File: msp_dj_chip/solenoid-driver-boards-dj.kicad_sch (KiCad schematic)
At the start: 0 parts

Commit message: updated changes
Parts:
- added C19: C_Small, symbol Device:C_Small
- added Q1: NMOS, symbol Simulation_SPICE:NMOS
- added R48: 30K, symbol Device:R_Small
- added R49: 500, symbol Device:R_Small
- added R50: 1K2, symbol Device:R_Small
- added R51, R52: 1, symbol Device:R_Small
- added R53: 0, symbol Device:R_Small
- added TP2, TP3, TP4, TP5, TP6: TestPoint, symbol Connector:TestPoint
- added U16: ${SIM.PARAMS}, symbol Simulation_SPICE:OPAMP
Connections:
- new net: R48.2, R49.1, TP2.1, U16.1 (+)
- new net: C19.2, Q1.2 (G), R51.2, R53.1, TP5.1
- new net: Q1.1 (D), TP6.1
- new net: C19.1, R53.2, U16.5
- new net: Q1.3 (S), R50.1, R50.2, R52.2, TP3.1, TP4.1, U16.2 (-)
- new net +24V: U16.3 (V+)
- new net GND: R49.2, R51.1, R52.1, U16.4 (V-)

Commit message: SOL-DRIVER-SHEET-ADDED
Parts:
- removed Q1: NMOS, symbol Simulation_SPICE:NMOS
- removed U16: ${SIM.PARAMS}, symbol Simulation_SPICE:OPAMP
- added C20, C21, C22, C23, C24, C25, C26, C27, C28, C29, C30, C31, C32, C33, C34: C_Small, symbol Device:C_Small
- added Q1, Q2, Q3, Q4, Q5, Q6, Q7, Q8: PMGD780SN, project_footprints:PMGD780SN, symbol Project_Symbols:2N-Channel_MOSFET
- added R100, R102, R120, R122, R124, R126, R54, R60, R62, R72, R74, R84, R86, R96, R98: 30K, symbol Device:R_Small
- added R101, R103, R121, R123, R125, R127, R55, R61, R63, R73, R75, R85, R87, R97, R99: 500, symbol Device:R_Small
- added R104, R105, R106, R107, R128, R129, R132, R133, R56, R64, R65, R76, R77, R88, R89: 1K2, symbol Device:R_Small
- added R108, R109, R110, R111, R130, R131, R134, R135, R57, R66, R67, R78, R79, R90, R91: 0, symbol Device:R_Small
- added R112, R113, R114, R115, R116, R117, R118, R119, R136, R137, R138, R139, R140, R141, R142, R143, R58, R59, R68, R69, R70, R71, R80, R81, R82, R83, R92, R93, R94, R95: 1, symbol Device:R_Small
- added TP10, TP11, TP12, TP13, TP14, TP15, TP16, TP17, TP18, TP19, TP20, TP21, TP22, TP23, TP24, TP25, TP26, TP27, TP28, TP29, TP30, TP31, TP32, TP33, TP34, TP35, TP36, TP37, TP38, TP39, TP40, TP41, TP42, TP43, TP44, TP45, TP46, TP47, TP48, TP49, TP50, TP51, TP52, TP53, TP54, TP55, TP56, TP57, TP58, TP59, TP60, TP61, TP62, TP63, TP64, TP65, TP66, TP67, TP68, TP69, TP7, TP70, TP71, TP72, TP73, TP74, TP75, TP76, TP77, TP78, TP79, TP8, TP80, TP81, TP9: TestPoint, symbol Connector:TestPoint
- added U16, U17, U18, U19, U20, U21, U22, U23: NCV272DMR2G, Package_SO:MSOP-8_3x3mm_P0.65mm, symbol Project_Symbols:OpAmp_NCV272
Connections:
- net +24V: now also U16.8 (VDD), U17.8 (VDD), U18.8 (VDD), U19.8 (VDD), U20.8 (VDD), U21.8 (VDD), U22.8 (VDD), U23.8 (VDD)
- net GND: now also R101.2, R103.2, R112.1, R113.1, R114.1, R115.1, R116.1, R117.1, R118.1, R119.1, R121.2, R123.2, R125.2, R127.2, R136.1, R137.1, R138.1, R139.1, R140.1, R141.1, R142.1, R143.1, R55.2, R58.1, R59.1, R61.2, R63.2, R68.1, R69.1, R70.1, R71.1, R73.2, R75.2, R80.1, R81.1, R82.1, R83.1, R85.2, R87.2, R92.1, R93.1, R94.1, R95.1, R97.2, R99.2, U16.4 (VSS), U17.4 (VSS), U18.4 (VSS), U19.4 (VSS), U20.4 (VSS), U21.4 (VSS), U22.4 (VSS), U23.4 (VSS)
- net at R48.2, R49.1, TP2.1: now also U16.2 (IN-1)
- net at C19.2, R51.2, R53.1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: now also Q2.2 (G1)
- net at TP6.1: now also Q2.6 (D1)
- net at C19.1, R53.2: now also U16.1 (OUT_1)
- net at R50.2, R52.2, TP4.1: now also Q2.1 (S1); no longer R50.1, TP3.1
- new net: C23.2, Q3.2 (G1), R78.1, R80.2, TP26.1
- new net: R72.2, R73.1, TP22.1, U18.2 (IN-1)
- new net: R60.2, R61.1, TP12.1, U17.2 (IN-1)
- new net: C21.2, Q1.2 (G1), R66.1, R68.2, TP16.1
- new net: C21.1, R66.2, U17.1 (OUT_1)
- new net: Q4.4 (S2), R89.2, R95.2, TP41.1
- new net: R96.2, R97.1, TP42.1, U20.2 (IN-1)
- new net: C26.2, Q4.5 (G2), R91.1, R93.2, TP37.1
- new net: R128.1, TP66.1, U22.3 (IN+1)
- new net: C25.2, Q4.2 (G1), R90.1, R92.2, TP36.1
- new net: Q3.6 (D1), TP28.1
- new net: R74.2, R75.1, TP23.1, U18.6 (IN-2)
- new net: Q1.6 (D1), TP18.1
- new net: C27.2, Q5.2 (G1), R108.1, R112.2, TP50.1
- new net: C27.1, R108.2, U20.1 (OUT_1)
- new net: R129.1, TP67.1, U22.5 (IN+2)
- new net: Q7.4 (S2), R129.2, R141.2, TP77.1
- new net: R105.1, TP47.1, U20.5 (IN+2)
- new net: Q8.1 (S1), R132.2, R142.2, TP79.1
- new net: C33.2, Q8.2 (G1), R134.1, R138.2, TP72.1
- new net: Q8.6 (D1), TP78.1
- new net: R126.2, R127.1, TP65.1, U23.6 (IN-2)
- new net: C25.1, R90.2, U19.1 (OUT_1)
- new net: R133.1, TP69.1, U23.5 (IN+2)
- new net: C34.1, R135.2, U23.7 (OUT_2)
- new net: R84.2, R85.1, TP32.1, U19.2 (IN-1)
- new net: R88.1, TP34.1, U19.3 (IN+1)
- new net: R89.1, TP35.1, U19.5 (IN+2)
- new net: R86.2, R87.1, TP33.1, U19.6 (IN-2)
- new net: C26.1, R91.2, U19.7 (OUT_2)
- new net: C24.1, R79.2, U18.7 (OUT_2)
- new net: C24.2, Q3.5 (G2), R79.1, R81.2, TP27.1
- new net: R107.1, TP49.1, U21.5 (IN+2)
- new net: R102.2, R103.1, TP45.1, U21.6 (IN-2)
- new net: C30.1, R111.2, U21.7 (OUT_2)
- new net: R76.1, TP24.1, U18.3 (IN+1)
- new net: C22.1, R67.2, U17.7 (OUT_2)
- new net: C22.2, Q1.5 (G2), R67.1, R69.2, TP17.1
- new net: C20.2, Q2.5 (G2), R57.1, R58.2, TP9.1
- new net: C20.1, R57.2, U16.7 (OUT_2)
- new net: Q3.1 (S1), R76.2, R82.2, TP29.1
- new net: Q8.3 (D2), TP80.1
- new net: Q8.4 (S2), R133.2, R143.2, TP81.1
- new net: C34.2, Q8.5 (G2), R135.1, R139.2, TP73.1
- new net: Q6.3 (D2), TP60.1
- new net: R104.1, TP46.1, U20.3 (IN+1)
- new net: C23.1, R78.2, U18.1 (OUT_1)
- new net: Q4.1 (S1), R88.2, R94.2, TP39.1
- new net: Q4.6 (D1), TP38.1
- new net: Q5.6 (D1), TP54.1
- new net: Q6.6 (D1), TP58.1
- new net: Q3.3 (D2), TP30.1
- new net: Q3.4 (S2), R77.2, R83.2, TP31.1
- new net: R98.2, R99.1, TP43.1, U20.6 (IN-2)
- new net: R65.1, TP15.1, U17.5 (IN+2)
- new net: R62.2, R63.1, TP13.1, U17.6 (IN-2)
- new net: Q2.3 (D2), TP10.1
- new net: Q1.4 (S2), R65.2, R71.2, TP21.1
- new net: Q7.1 (S1), R128.2, R140.2, TP75.1
- new net: C31.2, Q7.2 (G1), R130.1, R136.2, TP70.1
- new net: Q7.6 (D1), TP74.1
- new net: R100.2, R101.1, TP44.1, U21.2 (IN-1)
- new net: Q1.1 (S1), R64.2, R70.2, TP19.1
- new net: Q5.1 (S1), R104.2, R116.2, TP55.1
- new net: C33.1, R134.2, U23.1 (OUT_1)
- new net: R124.2, R125.1, TP64.1, U23.2 (IN-1)
- new net: R132.1, TP68.1, U23.3 (IN+1)
- new net: R77.1, TP25.1, U18.5 (IN+2)
- new net: R106.1, TP48.1, U21.3 (IN+1)
- new net: C30.2, Q6.5 (G2), R111.1, R115.2, TP53.1
- new net: R56.1, TP8.1, U16.5 (IN+2)
- new net: Q2.4 (S2), R56.2, R59.2, TP11.1
- new net: R120.2, R121.1, TP62.1, U22.2 (IN-1)
- new net: C31.1, R130.2, U22.1 (OUT_1)
- new net: Q6.1 (S1), R106.2, R118.2, TP59.1
- new net: C29.2, Q6.2 (G1), R110.1, R114.2, TP52.1
- new net: Q4.3 (D2), TP40.1
- new net: Q5.3 (D2), TP56.1
- new net: Q5.4 (S2), R105.2, R117.2, TP57.1
- new net: C28.2, Q5.5 (G2), R109.1, R113.2, TP51.1
- new net: R122.2, R123.1, TP63.1, U22.6 (IN-2)
- new net: R54.2, R55.1, TP7.1, U16.6 (IN-2)
- new net: R50.1, TP3.1, U16.3 (IN+1)
- new net: Q6.4 (S2), R107.2, R119.2, TP61.1
- new net: R64.1, TP14.1, U17.3 (IN+1)
- new net: C29.1, R110.2, U21.1 (OUT_1)
- new net: Q7.3 (D2), TP76.1
- new net: C32.2, Q7.5 (G2), R131.1, R137.2, TP71.1
- new net: C32.1, R131.2, U22.7 (OUT_2)
- new net: C28.1, R109.2, U20.7 (OUT_2)
- new net: Q1.3 (D2), TP20.1
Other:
- note added: "1 Ohm resistor should be +-1%"
- note added: "Dotted Square-> All in One Package"
- note added: "SOL_OUT_0-1"
- note added: "SOL_OUT_10-11"
- note added: "SOL_OUT_12-13"
- note added: "SOL_OUT_14-15"
- note added: "SOL_OUT_2-3"
- note added: "SOL_OUT_4-5"
- note added: "SOL_OUT_6-7"
- note added: "SOL_OUT_8-9"
- moved on the sheet: C19, R48, R49, R50, R51, R52, R53, TP2, TP3, TP4, TP5, TP6

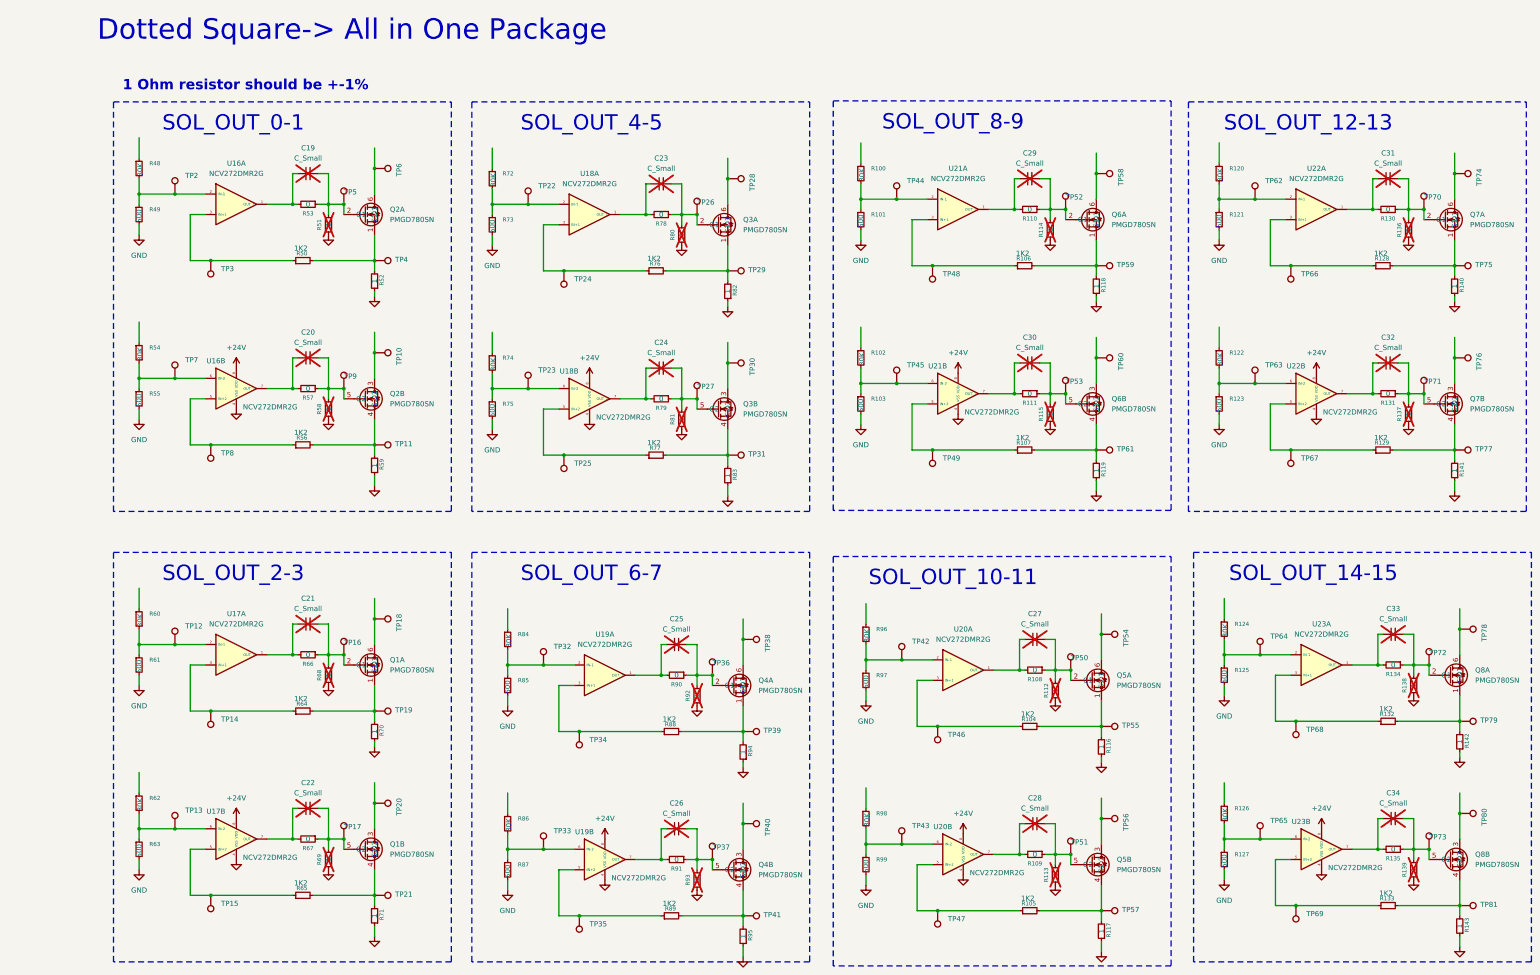
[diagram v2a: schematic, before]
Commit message: pin assignment adjustments - 16 adc
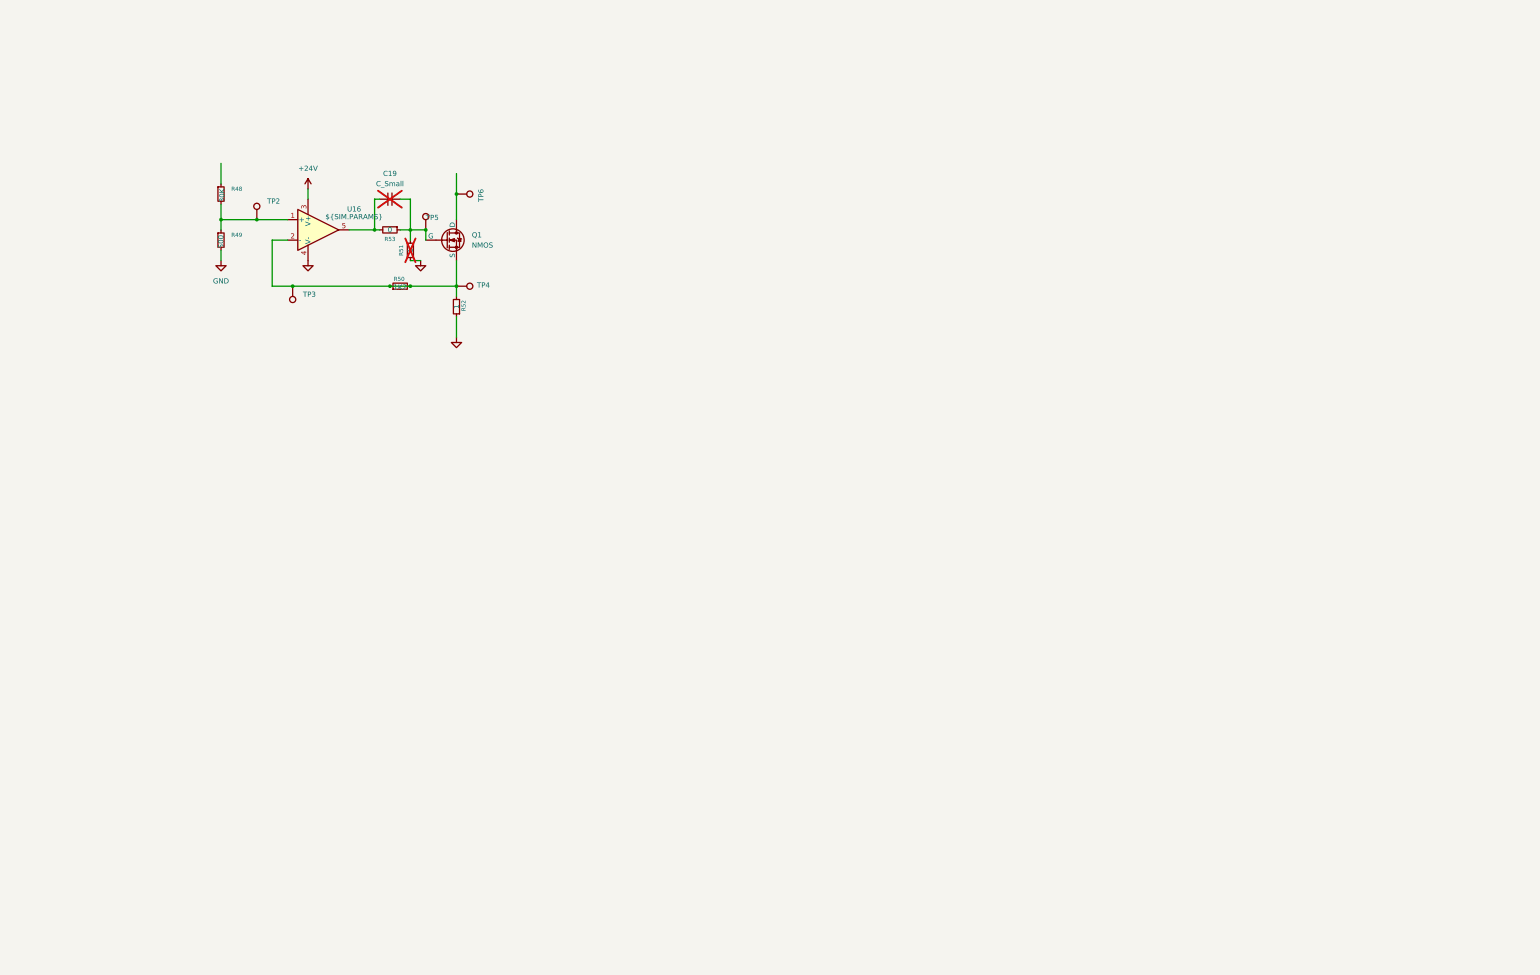
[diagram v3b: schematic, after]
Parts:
- removed C20, C21, C22, C23, C24, C25, C26, C27, C28, C29, C30, C31, C32, C33, C34: C_Small, symbol Device:C_Small
- removed Q1, Q2, Q3, Q4, Q5, Q6, Q7, Q8: PMGD780SN, project_footprints:PMGD780SN, symbol Project_Symbols:2N-Channel_MOSFET
- removed R100, R102, R120, R122, R124, R126, R54, R60, R62, R72, R74, R84, R86, R96, R98: 30K, symbol Device:R_Small
- removed R101, R103, R121, R123, R125, R127, R55, R61, R63, R73, R75, R85, R87, R97, R99: 500, symbol Device:R_Small
- removed R104, R105, R106, R107, R128, R129, R132, R133, R56, R64, R65, R76, R77, R88, R89: 1K2, symbol Device:R_Small
- removed R108, R109, R110, R111, R130, R131, R134, R135, R57, R66, R67, R78, R79, R90, R91: 0, symbol Device:R_Small
- removed R112, R113, R114, R115, R116, R117, R118, R119, R136, R137, R138, R139, R140, R141, R142, R143, R58, R59, R68, R69, R70, R71, R80, R81, R82, R83, R92, R93, R94, R95: 1, symbol Device:R_Small
- removed TP10, TP11, TP12, TP13, TP14, TP15, TP16, TP17, TP18, TP19, TP20, TP21, TP22, TP23, TP24, TP25, TP26, TP27, TP28, TP29, TP30, TP31, TP32, TP33, TP34, TP35, TP36, TP37, TP38, TP39, TP40, TP41, TP42, TP43, TP44, TP45, TP46, TP47, TP48, TP49, TP50, TP51, TP52, TP53, TP54, TP55, TP56, TP57, TP58, TP59, TP60, TP61, TP62, TP63, TP64, TP65, TP66, TP67, TP68, TP69, TP7, TP70, TP71, TP72, TP73, TP74, TP75, TP76, TP77, TP78, TP79, TP8, TP80, TP81, TP9: TestPoint, symbol Connector:TestPoint
- removed U16, U17, U18, U19, U20, U21, U22, U23: NCV272DMR2G, Package_SO:MSOP-8_3x3mm_P0.65mm, symbol Project_Symbols:OpAmp_NCV272
- added Q1: NMOS, symbol Simulation_SPICE:NMOS
- added U16: ${SIM.PARAMS}, symbol Simulation_SPICE:OPAMP
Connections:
- net +24V: now also U16.3 (V+)
- net GND: now also U16.4 (V-)
- net at R48.2, R49.1, TP2.1: now also U16.1 (+)
- net at C19.2, R51.2, R53.1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: now also Q1.2 (G)
- net at TP6.1: now also Q1.1 (D)
- net at C19.1, R53.2: now also U16.5
- net at R50.2, R52.2, TP4.1: now also R50.1, TP3.1, Q1.3 (S), U16.2 (-)
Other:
- note removed: "1 Ohm resistor should be +-1%"
- note removed: "Dotted Square-> All in One Package"
- note removed: "SOL_OUT_0-1"
- note removed: "SOL_OUT_10-11"
- note removed: "SOL_OUT_12-13"
- note removed: "SOL_OUT_14-15"
- note removed: "SOL_OUT_2-3"
- note removed: "SOL_OUT_4-5"
- note removed: "SOL_OUT_6-7"
- note removed: "SOL_OUT_8-9"
- moved on the sheet: C19, R48, R49, R50, R51, R52, R53, TP2, TP3, TP4, TP5, TP6
